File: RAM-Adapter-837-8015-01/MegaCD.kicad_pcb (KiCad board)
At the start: 4 copper layers, 59.3 x 29.2 mm, 7 parts, among them IC5 MB81C4256Z, IC6 MB81C4256Z, IC7 MB81C4256Z, IC8 MB81C4256Z, U1 HM514270

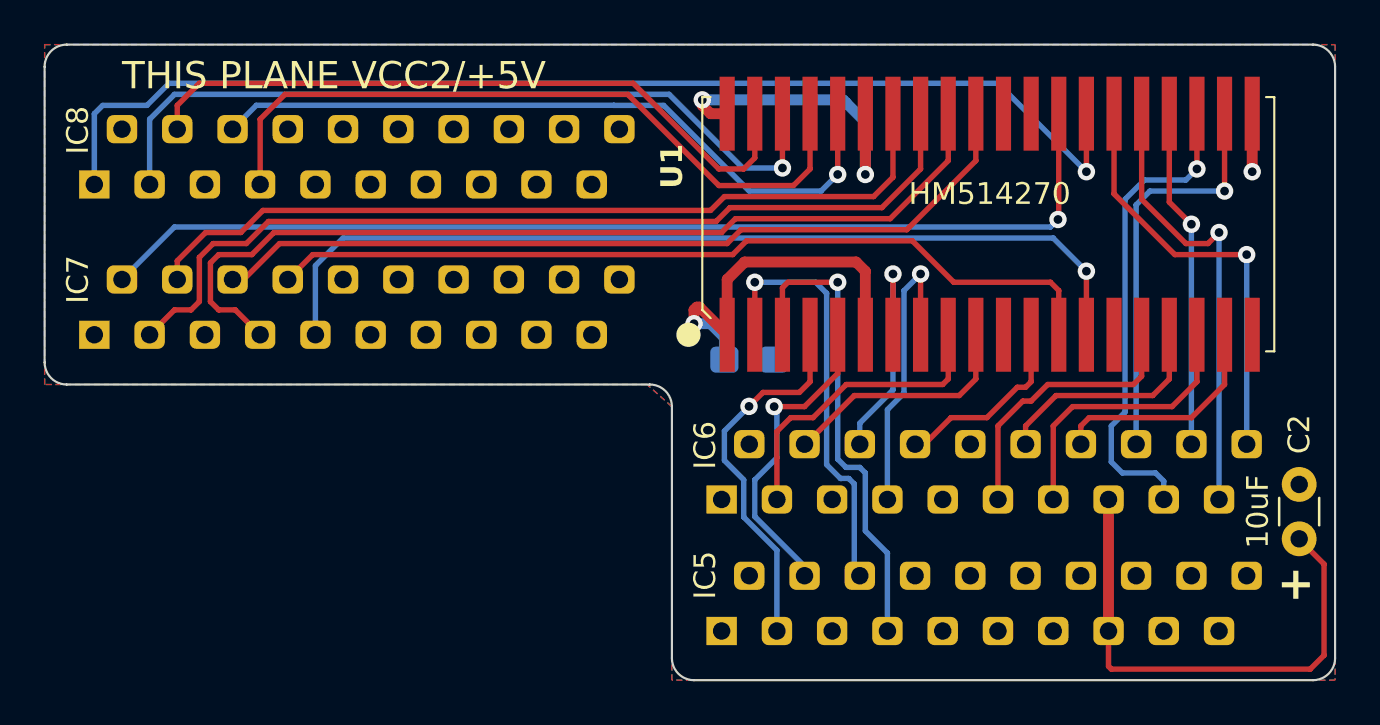
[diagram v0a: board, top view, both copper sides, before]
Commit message: Remove VCC planes from RAM adapter boards.
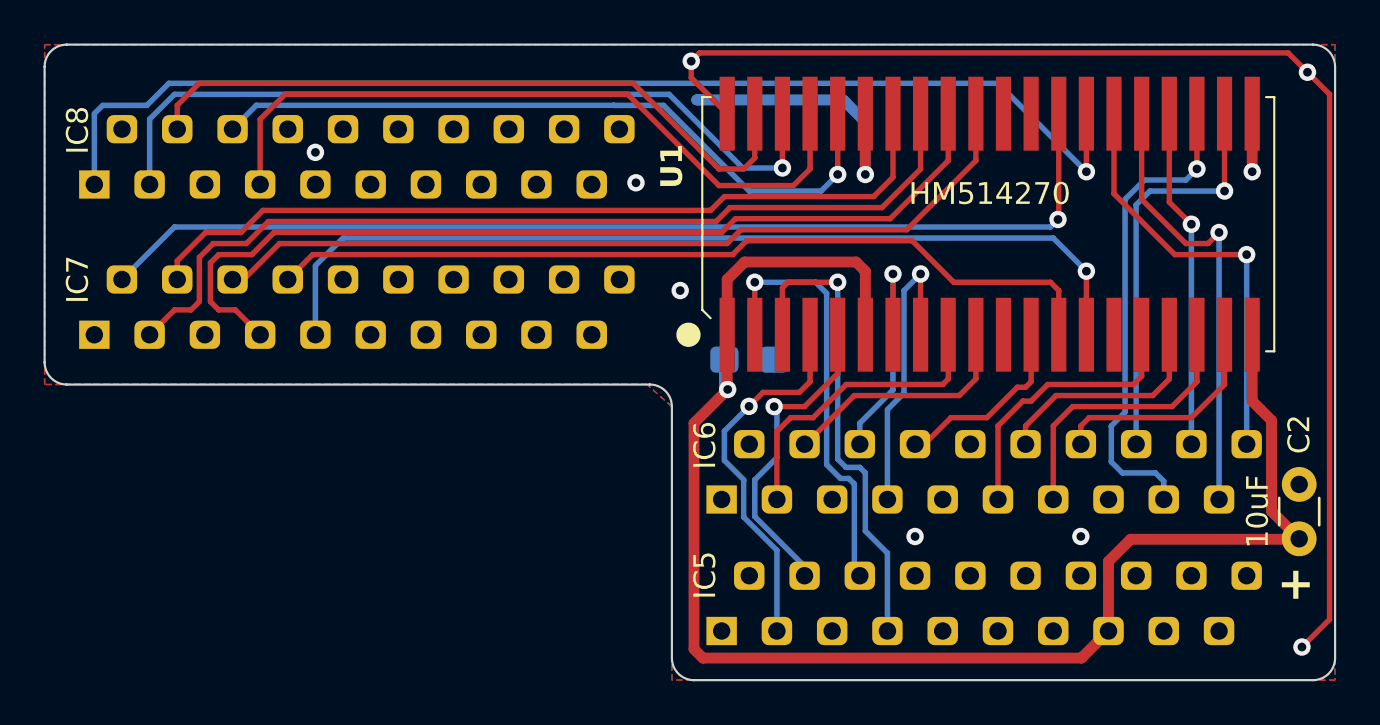
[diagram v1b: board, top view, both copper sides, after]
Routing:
- net VCC2: track 48.4 -> 127.6 mm
- net GND: track 30.3 -> 88.6 mm, vias 3 -> 10
- net PA4: track 75.6 -> 71.1 mm
- net PA6: track 71.3 -> 69.1 mm
- net PA5: track 78.0 -> 75.8 mm
- net PA7: track 74.9 -> 73.3 mm
- net ~{CLWE}: track 14.7 -> 15.6 mm
- net PA3: track 63.9 -> 64.5 mm
- added copper zone on F.Cu, net GND
- removed copper zone on F.Cu, net VCC2
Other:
- board text added: "DO NOT USE THIS LAYER FOR DRC PURPOSES ONLY"
- board text added: "ZIP-TO-SOJ DRAM ADAPTER FOR MEGA-CD 837-8015-01 REV 1.1 BY COSAM 08/2023"
- board text removed: "THIS PLANE VCC2/+5V"
- board text removed: "ZIP-TO-SOJ DRAM ADAPTER FOR MEGA-CD 837-8015-01 REV 1.0 BY COSAM 06/2023"
